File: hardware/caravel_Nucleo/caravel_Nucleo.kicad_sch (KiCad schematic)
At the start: 64 parts, among them J10 PinHeader_1x11, J11 PinHeader_1x02, J12 PinHeader_1x02, J3 PinHeader_1x02, J4 836-22-004-10-001101, J5 PinHeader_1x02, J6 PinHeader_1x02, J7 836-22-006-10-001101, J8 640456-3, J9 640456-3, SW1 KMR2, T1 Logo, T2 Logo, U10 MCP4661, U12 NUCLEO144-F746ZG, U4 MAX811REUS+T, U5 TAR5S33UTE85LF, U6 TAR5S18U(TE85L,F), U7 W25Q32FVSS, U8 caravel_breakout, U9 MIC2211-AAYML-TR, X1 ECS-2520MVLC-100-BN-TR

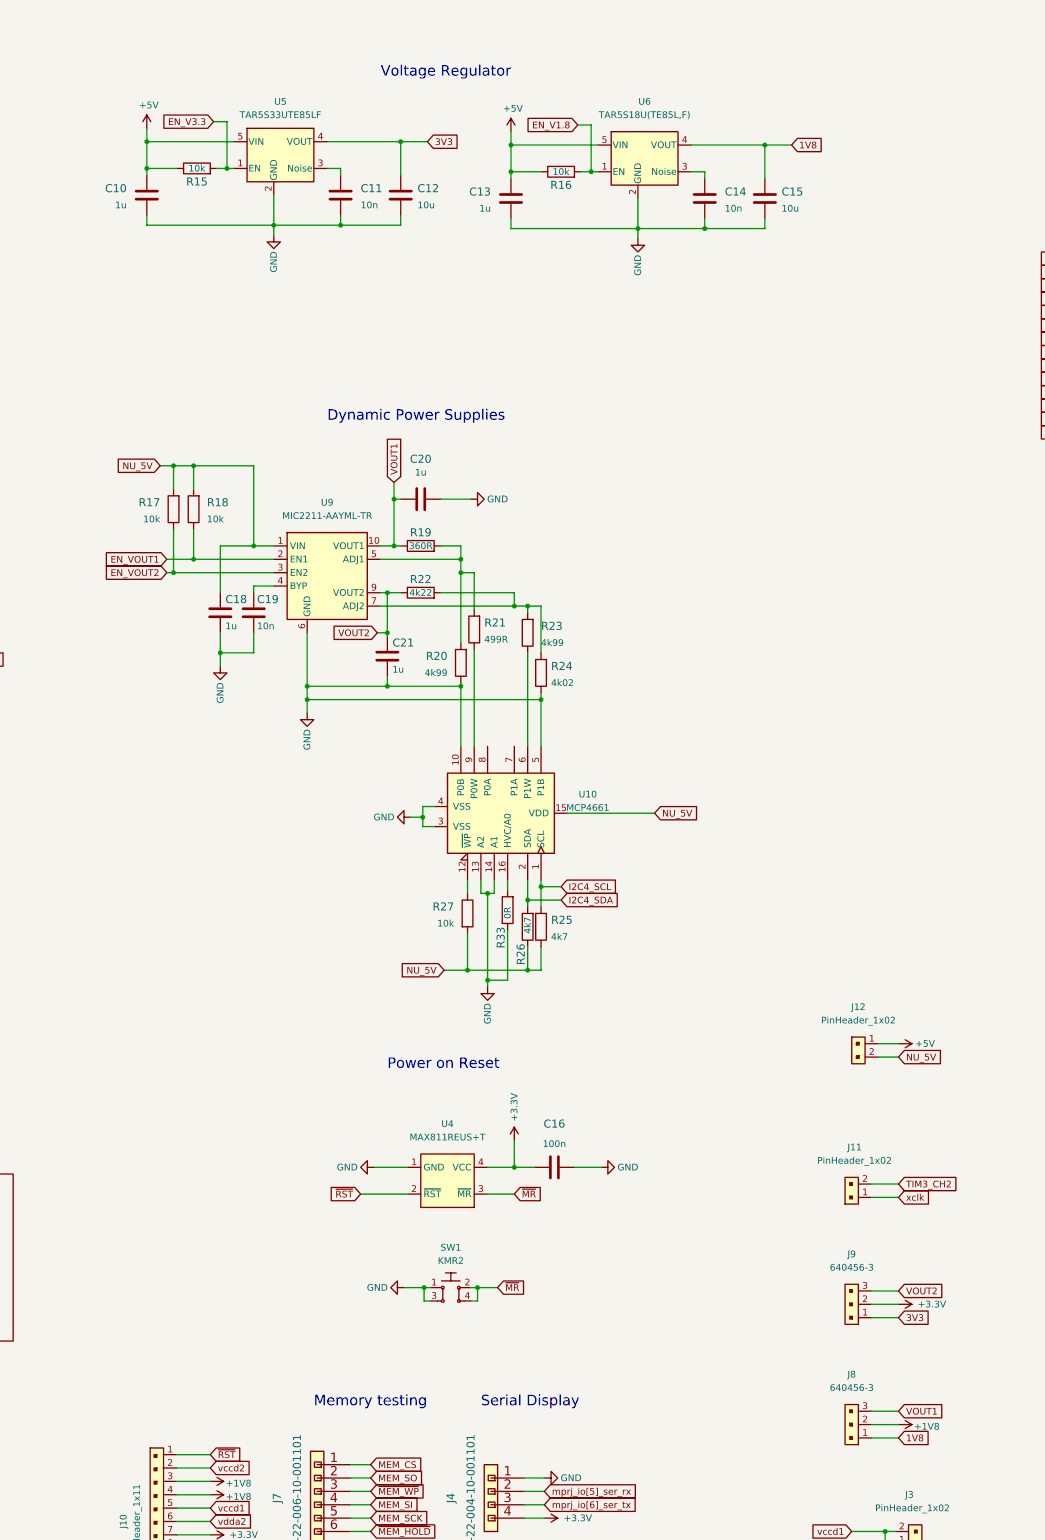
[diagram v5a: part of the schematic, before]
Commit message: Simplfy power supply
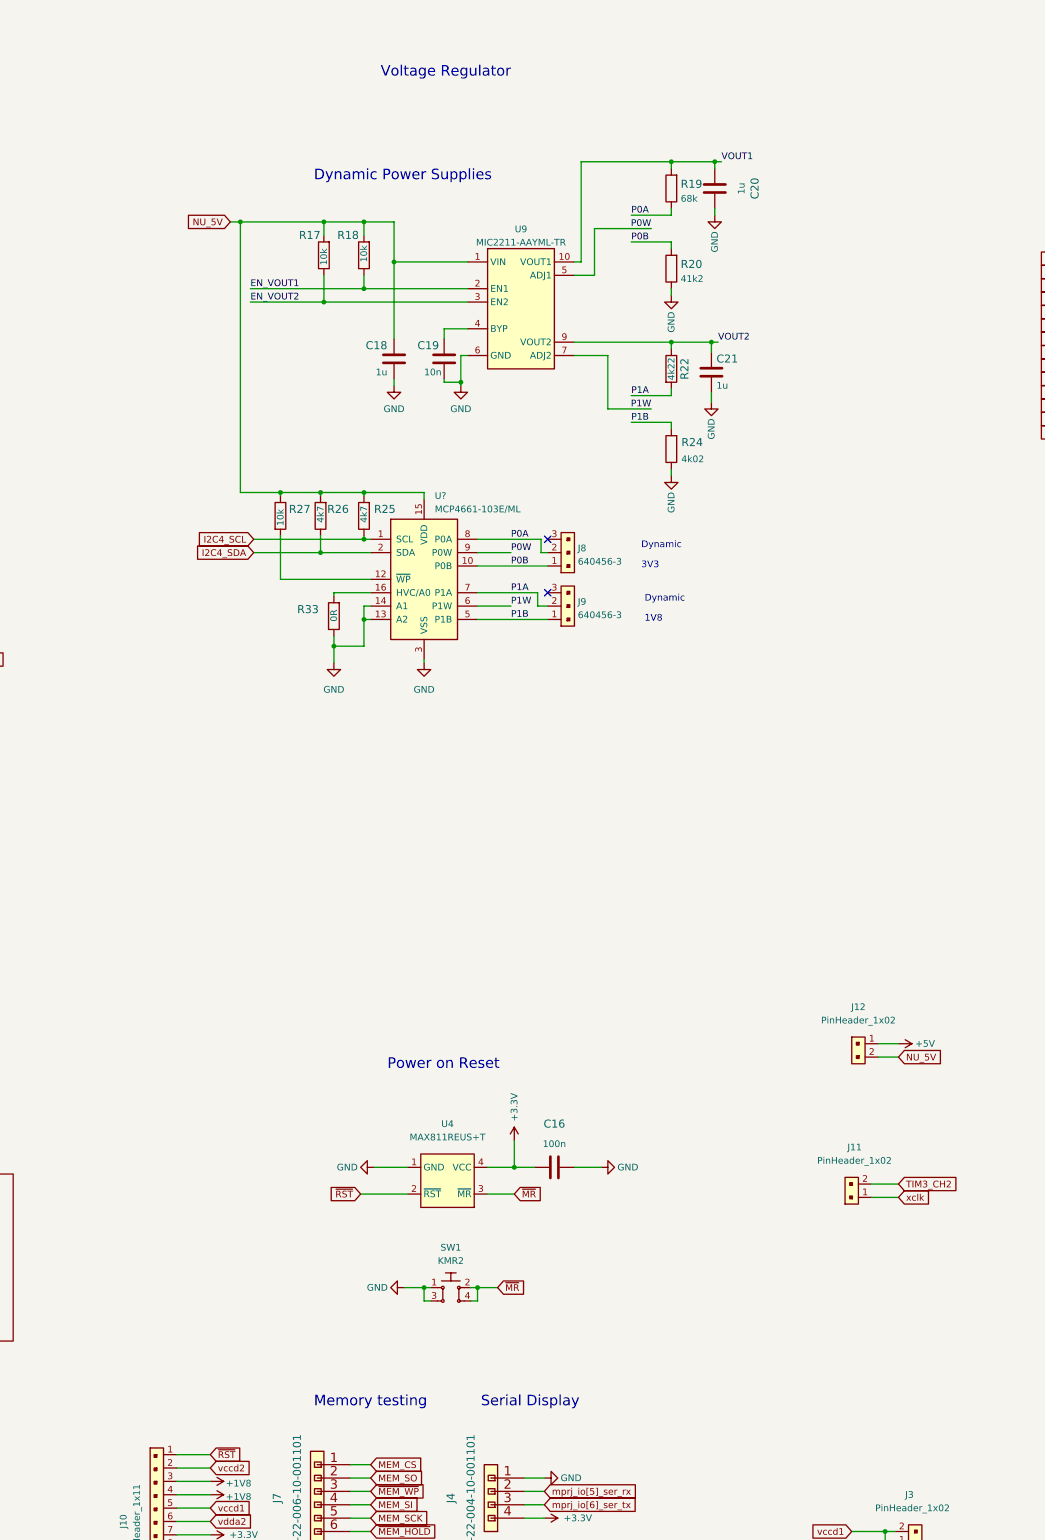
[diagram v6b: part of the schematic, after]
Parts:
- removed C10, C13: C_1u_0603, antmicro-footprints:0603-cap, symbol antmicroCapacitors0603:C_1u_0603
- removed C11, C14: C_10n_0603, antmicro-footprints:0603-cap, symbol antmicroCapacitors0603:C_10n_0603
- removed C12, C15: C_10u_0603, antmicro-footprints:0603-cap, symbol antmicroCapacitors0603:C_10u_0603
- removed R15, R16: R_10k_0603, antmicro-footprints:0603-res, symbol antmicroResistors0603:R_10k_0603
- removed R19: R_360R_0603, antmicro-footprints:0603-res, symbol antmicroResistors0603:R_360R_0603
- removed R20, R23: R_4k99_0603, antmicro-footprints:0603-res, symbol antmicroResistors0603:R_4k99_0603
- removed R21: R_499R_0603, antmicro-footprints:0603-res, symbol antmicroResistors0603:R_499R_0603
- removed U10: MCP4661, antmicro-footprints:QFN-16_EP_4x4_Pitch0.65mm, symbol antmicroInterfaceIOExpanders:MCP4661
- removed U5: TAR5S33UTE85LF, antmicro-footprints:SOT-353, symbol antmicroPMICVoltageRegulatorsLinear:TAR5S33UTE85LF
- removed U6: TAR5S18U(TE85L,F), antmicro-footprints:SOT-353, symbol antmicroPMICVoltageRegulatorsLinear:TAR5S18U(TE85L,F)
- added R19: R_68k_0603, antmicro-footprints:0603-res, symbol antmicroResistors0603:R_68k_0603
- added R20: R_41k2_0603, antmicro-footprints:0603-res, symbol antmicroResistors0603:R_41k2_0603
- added U?: MCP4661-103E/ML, antmicro-footprints:QFN-16_EP_4x4_Pitch0.65mm, symbol antmicroInterfaceIOExpanders:MCP4661-103E/ML
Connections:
- net +1V8: no longer J8.2
- net +3V3: no longer J9.2
- net GND: now also R20.1, U?.13 (A2), U?.14 (A1), U?.3 (VSS), U?.4 (VSS)
- net I2C4_SCL: now also R25.1, U?.1 (SCL); no longer R25.2
- net I2C4_SDA: now also R26.1, U?.2 (SDA); no longer R26.2
- net NU_5V: now also R25.2, R26.2, R27.1, U?.15 (VDD); no longer R25.1, R26.1, R27.2
- net VOUT1: now also R19.2; no longer J8.3
- net VOUT2: no longer J9.3
- net P0W: now reaches U9.5 (ADJ1)
- net P0W: now also U?.9 (P0W)
- net at R33.2: now also U?.16 (HVC/A0)
- net 1V8 renamed P0B
- net P0B: now also R20.2, U?.10 (P0B)
- net 3V3 renamed P1B
- net P1B: now also R24.2, U?.5 (P1B)
- new net: R27.2, U?.12 (~{WP})
- new net P0A: J8.2, R19.1, U?.8 (P0A)
- new net P1A: J9.2, R22.2, U?.7 (P1A)
- new net P1W: U9.7 (ADJ2), U?.6 (P1W)
- no-connect marks 35 -> 37
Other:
- note added: "1V8"
- note added: "3V3"
- note added: "Dynamic"
- moved on the sheet: C18, C19, C20, C21, J8, J9, R17, R18, R22, R24, R25, R26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

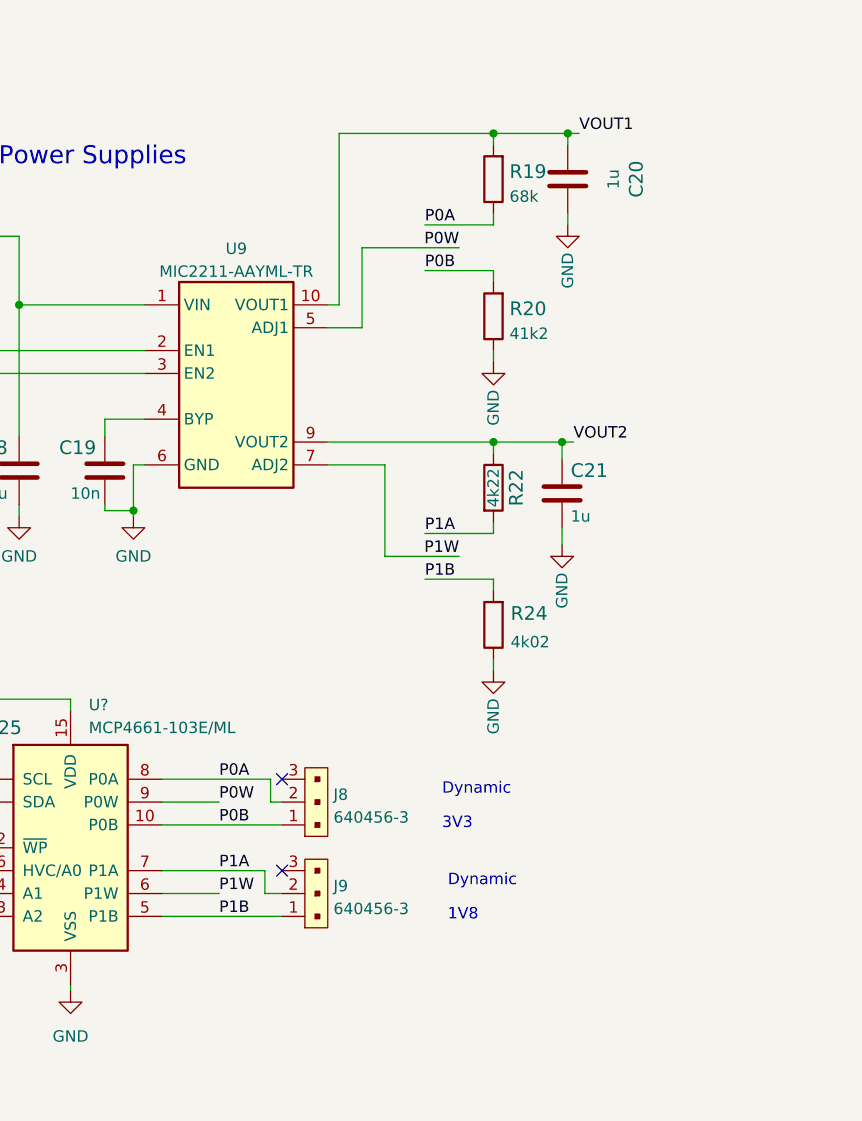
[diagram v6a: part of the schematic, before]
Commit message: Adjust divider, add 1V8 LV option
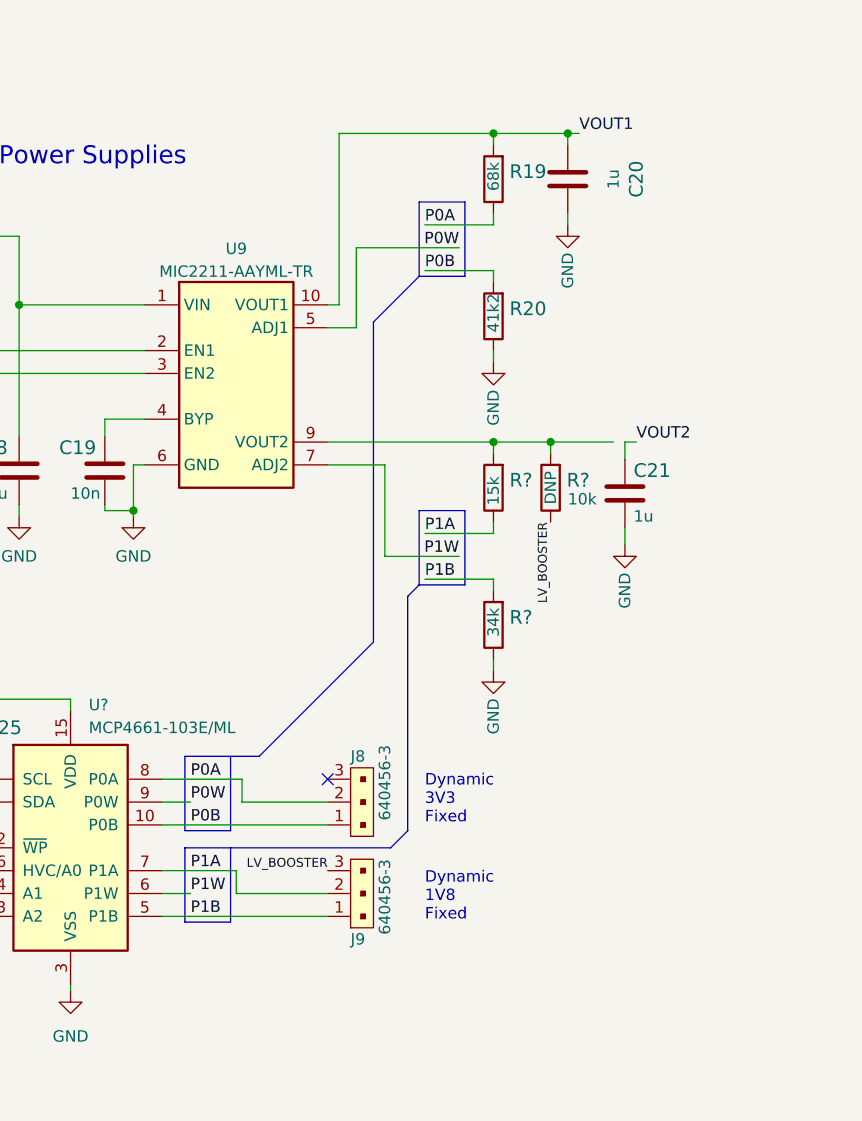
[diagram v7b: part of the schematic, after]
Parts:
- removed R22: R_4k22_0603, antmicro-footprints:0603-res, symbol antmicroResistors0603:R_4k22_0603
- removed R24: R_4k02_0402, antmicro-footprints:0402-res, symbol antmicroResistors0402:R_4k02_0402
- added R?: R_15k_0603, antmicro-footprints:0603-res, symbol antmicroResistors0603:R_15k_0603
- added R?: R_34k_0402, antmicro-footprints:0402-res, symbol antmicroResistors0402:R_34k_0402
- added R?: R_10k_0603, antmicro-footprints:0603-res, symbol antmicroResistors0603:R_10k_0603
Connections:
- net GND: now also R?.1
- net P1A: now also R?.1
- net P1B: now also R?.2
- net VOUT2: no longer U9.9 (VOUT2)
- net LV_BOOSTER: now reaches J9.3
- net LV_BOOSTER: now also R?.1
- new net: R?.2, R?.2, U9.9 (VOUT2)
- no-connect marks 37 -> 36
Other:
- note added: "Dynamic 1V8 Fixed"
- note added: "Dynamic 3V3 Fixed"
- note removed: "1V8"
- note removed: "3V3"
- note removed: "Dynamic"
- moved on the sheet: C21, J8, J9

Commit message: Tidy up schematic connections
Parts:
- removed D3, D4: LTST-C150KGKT, antmicro-footprints:LED-1206, symbol antmicroLEDIndicationDiscrete:LTST-C150KGKT
- removed R13, R14: R_82R_0603, antmicro-footprints:0603-res, symbol antmicroResistors0603:R_82R_0603
- added C1: C_10n_0402, antmicro-footprints:0402-cap, symbol antmicroCapacitors0402:C_10n_0402
- added C2, C3, C4, C5, C6, C7, C8, C? (x2): C_100n_0603, antmicro-footprints:0603-cap, symbol antmicroCapacitors0603:C_100n_0603
- added C? (x2): C_18p_0603, antmicro-footprints:0603-cap, symbol antmicroCapacitors0603:C_18p_0603
- added C? (x2): C_4u7_0603, antmicro-footprints:0603-cap, symbol antmicroCapacitors0603:C_4u7_0603
- added D1, D2, D3, D4: KP-1608ZGC, antmicro-footprints:LED_0603, symbol antmicroLEDIndicationDiscrete:KP-1608ZGC
- added J1: USB4105-GF-A, antmicro-footprints:GCT_USB4105-GF-A, symbol antmicroUSBDVIHDMIConnectors:USB4105-GF-A
- added J?: M20-9990246, antmicro-footprints:PinHeader_1x2_P2.54mm, symbol antmicroRectangularConnectorsHeadersMalePins:M20-9990246
- added R1: R_10k_0402, antmicro-footprints:0402-res, symbol antmicroResistors0402:R_10k_0402
- added R13, R14, R3, R4: R_470R_0603, antmicro-footprints:0603-res, symbol antmicroResistors0603:R_470R_0603
- added R2: R_12k_0402, antmicro-footprints:0402-res, symbol antmicroResistors0402:R_12k_0402
- added R? (x2): R_5k1_0402, antmicro-footprints:0402-res, symbol antmicroResistors0402:R_5k1_0402
- added R?: R_10k_0603, antmicro-footprints:0603-res, symbol antmicroResistors0603:R_10k_0603
- added U1: FT232HQ, antmicro-footprints:QFN-48-1EP_6x6mm, symbol antmicroInterfaceControllers:FT232HQ
- added U2, U3: SN74LVC1G125DCKR, antmicro-footprints:SOT-353, symbol antmicroLogicBuffersDriversReceiversTransceivers:SN74LVC1G125DCKR
- added Y1: ABM8G-12.000MHZ-18-D2Y-T, antmicro-footprints:KX-7, symbol antmicroCrystals:ABM8G-12.000MHZ-18-D2Y-T
- U12: value NUCLEO144-F746ZG -> NUCLEO144-F429ZI; footprint Module:ST_Morpho_Connector_144_STLink -> antmicro-footprints:ST_Morpho_Connectors_144; symbol MCU_Module:NUCLEO144-F746ZG -> antmicroModules:NUCLEO144-F429ZI; MPN (none) -> NUCLEO-F429ZI; Manufacturer (none) -> STMicroelectronics
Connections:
- net VOUT1 is gone; now on net +3V3: C20.1, R19.2, U9.10 (VOUT1)
- net VOUT2 is gone; now on net +1V8: C21.1
- net +1V8: now also R?.2, R?.2, U9.9 (VOUT2)
- net +3V3: now also R13.2, R14.2, R?.2, U3.5 (VCC)
- net SPI5_CS: now also U1.16 (ADBUS3)
- net SPI5_MISO: now also U1.15 (ADBUS2)
- net SPI5_MOSI: now also U1.14 (ADBUS1), U2.4 (Y)
- net SPI5_SCK: now also U1.13 (ADBUS0), U3.2 (A)
- net UART8_RX: now also U2.2 (A)
- net UART8_TX: now also U3.4 (Y)
- net gpio: now also D3.2
- net ~{MR}: now also U1.25 (ACBUS1)
- net GND renamed AGND
- net AGND: now also C1.2, C2.1, C3.1, C4.2, C5.2, C6.2, C7.2, C8.2, C?.1, C?.1, C?.2, C?.2, C?.2, C?.2, D4.2, J1.A1 (GND), J1.A12 (GND), J1.B1 (GND), J1.B12 (GND), J?.1, R2.1, R?.2, R?.2, U1.10 (GND), U1.11 (GND), U1.22 (GND), U1.23 (GND), U1.35 (GND), U1.36 (GND), U1.4 (AGND), U1.41 (AGND), U1.42 (TEST), U1.47 (GND), U1.48 (GND), U1.49 (EP), U1.9 (AGND), U2.3 (GND), U3.3 (GND), Y1.2, Y1.4
- new net: D4.1, R14.1
- new net: D3.1, R13.1
- new net: D1.2, R3.2
- new net: D2.2, R4.2
- new net CC1: J1.A5 (CC1), R?.1
- new net CC2: J1.B5 (CC2), R?.1
- new net EN_1V8: U1.29 (ACBUS5)
- new net EN_3V3: U1.30 (ACBUS6)
- new net FTDI_3V3: C4.1, C5.1, C6.1, C7.1, C8.1, C?.1, C?.2, D1.1, D2.1, R1.2, U1.12 (VCCIO), U1.24 (VCCIO), U1.3 (VPHY), U1.39 (VCCD), U1.46 (VCCIO), U1.8 (VPLL), U2.5 (VCC)
- new net FTDI_DN: U1.6 (DM)
- new net FTDI_DP: U1.7 (DP)
- new net FTDI_RESET: C1.1, R1.1, U1.34 (~{RESET})
- new net REF: R2.2, U1.5 (REF)
- new net USB_DN: J1.A7 (D-), J1.B7 (D-)
- new net USB_DP: J1.A6 (D+), J1.B6 (D+)
- new net VBUS: C?.1, C?.2, J1.A4 (VBUS), J1.A9 (VBUS), J1.B4 (VBUS), J1.B9 (VBUS), U1.40 (VREGIN)
- new net VCCA: C3.2, U1.37 (VCCA)
- new net VCORE: C2.2, U1.38 (VCCCORE)
- new net XIN: C?.1, U1.1 (XCSI), Y1.1
- new net XOUT: C?.1, U1.2 (XCSO), Y1.3
- new net ~{RX_LED}: R4.1, U1.26 (ACBUS2)
- new net ~{TX_LED}: R3.1, U1.27 (ACBUS3)
- new net ~{UART_EN}: J?.2, R?.1, U1.21 (ACBUS0), U2.1 (~{OE}), U3.1 (~{OE})
- no-connect marks 36 -> 90
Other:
- removed sheet FTDI
- note added: "Buffers to enable FTDI UART interface"
- note added: "FTDI Module"
- note added: "LDO OUT"
- note removed: "Voltage Regulator"
- moved on the sheet: C16, C17, C18, C19, C20, C21, C9, J10, J11, J12, J4, J5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
